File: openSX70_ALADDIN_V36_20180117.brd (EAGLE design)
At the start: 95.9 x 27.9 mm, 47 parts, among them Q1 5.8A/30V/35mΩ, Q2 5.8A/30V/35mΩ, U1 ATMEGA328P_TQFP, U3 BH1750FVI-TR, Y1 CSTCE16M0V53-R0

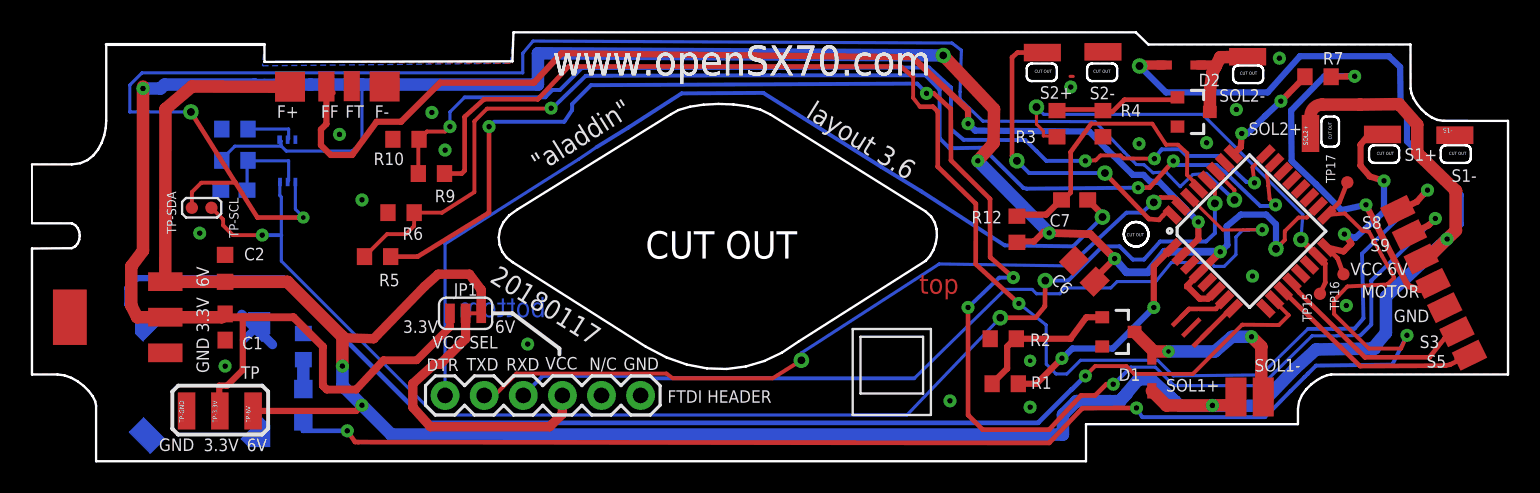
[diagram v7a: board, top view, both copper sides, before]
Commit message: Cosmetic changes and moved some files (chocolate) to OLD folder.
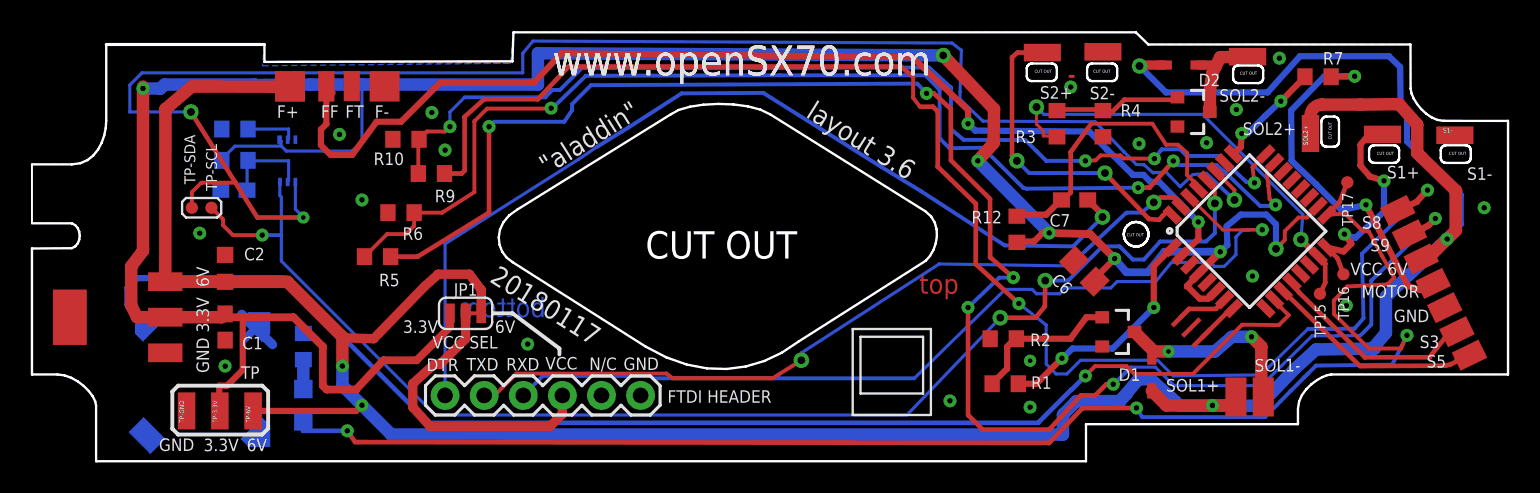
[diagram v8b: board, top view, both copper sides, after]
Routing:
- net GND: vias 17 -> 18
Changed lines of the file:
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@@
 <layer number="14" name="Route14" color="1" fill="6" visible="no" active="no"/>
 <layer number="15" name="Route15" color="4" fill="6" visible="no" active="no"/>
-<layer number="16" name="Bottom" color="1" fill="1" visible="no" active="yes"/>
+<layer number="16" name="Bottom" color="1" fill="1" visible="yes" active="yes"/>
 <layer number="17" name="Pads" color="2" fill="1" visible="yes" active="yes"/>
 <layer number="18" name="Vias" color="2" fill="1" visible="yes" active="yes"/>
@@
 <layer number="20" name="Dimension" color="24" fill="1" visible="yes" active="yes"/>
 <layer number="21" name="tPlace" color="7" fill="1" visible="yes" active="yes"/>
-<layer number="22" name="bPlace" color="7" fill="1" visible="no" active="yes"/>
+<layer number="22" name="bPlace" color="7" fill="1" visible="yes" active="yes"/>
 <layer number="23" name="tOrigins" color="15" fill="1" visible="yes" active="yes"/>
-<layer number="24" name="bOrigins" color="15" fill="1" visible="no" active="yes"/>
+<layer number="24" name="bOrigins" color="15" fill="1" visible="yes" active="yes"/>
 <layer number="25" name="tNames" color="7" fill="1" visible="yes" active="yes"/>
-<layer number="26" name="bNames" color="7" fill="1" visible="no" active="yes"/>
+<layer number="26" name="bNames" color="7" fill="1" visible="yes" active="yes"/>
 <layer number="27" name="tValues" color="7" fill="1" visible="no" active="yes"/>
 <layer number="28" name="bValues" color="7" fill="1" visible="no" active="yes"/>
@@
 <layer number="38" name="bTest" color="7" fill="1" visible="no" active="yes"/>
 <layer number="39" name="tKeepout" color="4" fill="11" visible="yes" active="yes"/>
-<layer number="40" name="bKeepout" color="1" fill="11" visible="no" active="yes"/>
+<layer number="40" name="bKeepout" color="1" fill="11" visible="yes" active="yes"/>
 <layer number="41" name="tRestrict" color="4" fill="10" visible="yes" active="yes"/>
-<layer number="42" name="bRestrict" color="1" fill="10" visible="no" active="yes"/>
+<layer number="42" name="bRestrict" color="1" fill="10" visible="yes" active="yes"/>
 <layer number="43" name="vRestrict" color="2" fill="10" visible="no" active="yes"/>
-<layer number="44" name="Drills" color="7" fill="1" visible="no" active="yes"/>
+<layer number="44" name="Drills" color="7" fill="1" visible="yes" active="yes"/>
 <layer number="45" name="Holes" color="7" fill="1" visible="yes" active="yes"/>
 <layer number="46" name="Milling" color="3" fill="1" visible="no" active="yes"/>
@@
 <layer number="50" name="dxf" color="7" fill="1" visible="no" active="no"/>
 <layer number="51" name="tDocu" color="7" fill="1" visible="yes" active="yes"/>
-<layer number="52" name="bDocu" color="7" fill="1" visible="no" active="yes"/>
+<layer number="52" name="bDocu" color="7" fill="1" visible="yes" active="yes"/>
 <layer number="53" name="tGND_GNDA" color="7" fill="9" visible="no" active="no"/>
 <layer number="54" name="bGND_GNDA" color="1" fill="9" visible="no" active="no"/>
@@
 <text x="75.72375" y="5.334" size="0.8128" layer="21" font="vector" ratio="20">SOL1+</text>
 <text x="81.4705" y="6.63575" size="0.8128" layer="21" font="vector" ratio="20">SOL1-</text>
-<text x="81.0895" y="22.00275" size="0.8128" layer="21" font="vector" ratio="20">SOL2+</text>
-<text x="91.21775" y="20.32" size="0.8128" layer="21" font="vector" ratio="20">S1+</text>
-<text x="94.26575" y="18.95475" size="0.8128" layer="21" font="vector" ratio="20">S1-</text>
+<text x="80.7085" y="22.00275" size="0.8128" layer="21" font="vector" ratio="20">SOL2+</text>
+<text x="90.07475" y="19.177" size="0.8128" layer="21" font="vector" ratio="20">S1+</text>
+<text x="95.28175" y="19.08175" size="0.8128" layer="21" font="vector" ratio="20">S1-</text>
 <text x="67.53225" y="24.35225" size="0.8128" layer="21" font="vector" ratio="20">S2+</text>
 <text x="70.77075" y="24.3205" size="0.8128" layer="21" font="vector" ratio="20">S2-</text>
@@
 <wire x1="59.944" y1="5.207" x2="55.88" y2="5.207" width="0.1524" layer="21"/>
 <wire x1="55.88" y1="5.207" x2="55.88" y2="8.89" width="0.1524" layer="21"/>
-<text x="40.4495" y="24.41575" size="1.27" layer="21" font="vector" ratio="15" rot="R212">"aladdin"</text>
+<text x="40.9575" y="24.28875" size="1.27" layer="21" font="vector" ratio="15" rot="R212">"aladdin"</text>
 <wire x1="12.065" y1="17.907" x2="14.097" y2="17.907" width="0.1524" layer="21"/>
 <wire x1="14.097" y1="17.907" x2="14.351" y2="17.653" width="0.1524" layer="21"/>
@@
 <element name="TP-GND" library="openSX70" package="SX70-S-PAD2" value="SX70-S-PAD-NEW" x="12.192" y="4.064" rot="R90"/>
 <element name="TP15" library="testpad" library_urn="urn:adsk.eagle:library:385" package="TP08R" package3d_urn="urn:adsk.eagle:package:27956/1" value="PTR1TP08R" x="85.725" y="11.684" smashed="yes">
-<attribute name="NAME" x="85.1979" y="9.86" size="0.6096" layer="25" font="vector" ratio="12" rot="R90"/>
+<attribute name="NAME" x="86.0869" y="8.844" size="0.7112" layer="25" font="vector" ratio="12" rot="R90"/>
 <attribute name="TP_SIGNAL_NAME" value="" x="85.725" y="9.779" size="1" layer="37"/>
 <attribute name="VALUE" x="85.344" y="11.303" size="0.0254" layer="27"/>
 </element>
 <element name="TP16" library="testpad" library_urn="urn:adsk.eagle:library:385" package="TP08R" package3d_urn="urn:adsk.eagle:package:27956/1" value="PTR1TP08R" x="87.249" y="12.954" smashed="yes">
-<attribute name="NAME" x="86.9759" y="10.622" size="0.6096" layer="25" font="vector" ratio="12" rot="R90"/>
+<attribute name="NAME" x="87.6109" y="9.987" size="0.7112" layer="25" font="vector" ratio="12" rot="R90"/>
 <attribute name="TP_SIGNAL_NAME" value="" x="87.249" y="11.049" size="1" layer="37"/>
 <attribute name="VALUE" x="86.868" y="12.573" size="0.0254" layer="27"/>
 </element>
 <element name="TP17" library="testpad" library_urn="urn:adsk.eagle:library:385" package="TP08R" package3d_urn="urn:adsk.eagle:package:27956/1" value="PTR1TP08R" x="87.503" y="18.923" smashed="yes">
-<attribute name="NAME" x="86.7219" y="18.877" size="0.6096" layer="25" font="vector" ratio="12" rot="R90"/>
+<attribute name="NAME" x="87.8649" y="16.083" size="0.7112" layer="25" font="vector" ratio="12" rot="R90"/>
 <attribute name="TP_SIGNAL_NAME" value="" x="87.503" y="17.018" size="1" layer="37"/>
 <attribute name="VALUE" x="87.122" y="18.542" size="0.0254" layer="27"/>
 </element>
 <element name="TP-SDA" library="testpad" library_urn="urn:adsk.eagle:library:385" package="TP08R" package3d_urn="urn:adsk.eagle:package:27956/1" value="PTR1TP08R" x="12.446" y="17.272" smashed="yes">
-<attribute name="NAME" x="10.8141" y="18.334" size="0.6096" layer="25" font="vector" ratio="12" rot="R270"/>
+<attribute name="NAME" x="11.9571" y="22.017" size="0.7112" layer="25" font="vector" ratio="12" rot="R270"/>
 <attribute name="TP_SIGNAL_NAME" value="" x="12.446" y="15.367" size="1" layer="37"/>
 <attribute name="VALUE" x="12.065" y="16.891" size="0.0254" layer="27"/>
 </element>
 <element name="TP-SCL" library="testpad" library_urn="urn:adsk.eagle:library:385" package="TP08R" package3d_urn="urn:adsk.eagle:package:27956/1" value="PTR1TP08R" x="13.716" y="17.272" smashed="yes">
-<attribute name="NAME" x="15.4749" y="15.321" size="0.6096" layer="25" font="vector" ratio="12" rot="R90"/>
+<attribute name="NAME" x="14.0779" y="18.369" size="0.7112" layer="25" font="vector" ratio="12" rot="R90"/>
 <attribute name="TP_SIGNAL_NAME" value="" x="13.716" y="15.367" size="1" layer="37"/>
 <attribute name="VALUE" x="13.335" y="16.891" size="0.0254" layer="27"/>
@@
 <contactref element="TP-GND" pad="P$1"/>
 <via x="61.69025" y="4.73075" extent="1-16" drill="0.35"/>
+<via x="96.393" y="17.272" extent="1-16" drill="0.35"/>
 </signal>
 <signal name="6V">
